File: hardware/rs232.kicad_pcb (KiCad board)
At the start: 2 copper layers, 45 x 35 mm, 33 parts, among them J1 DB9, P1 CON-SENSOR, P2 CONN_5, P3 CONN_5, U1 M24C64, U2 SC16IS740, U3 SP3232EBCN, U4 DRILL, U5 DRILL, U6 DRILL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

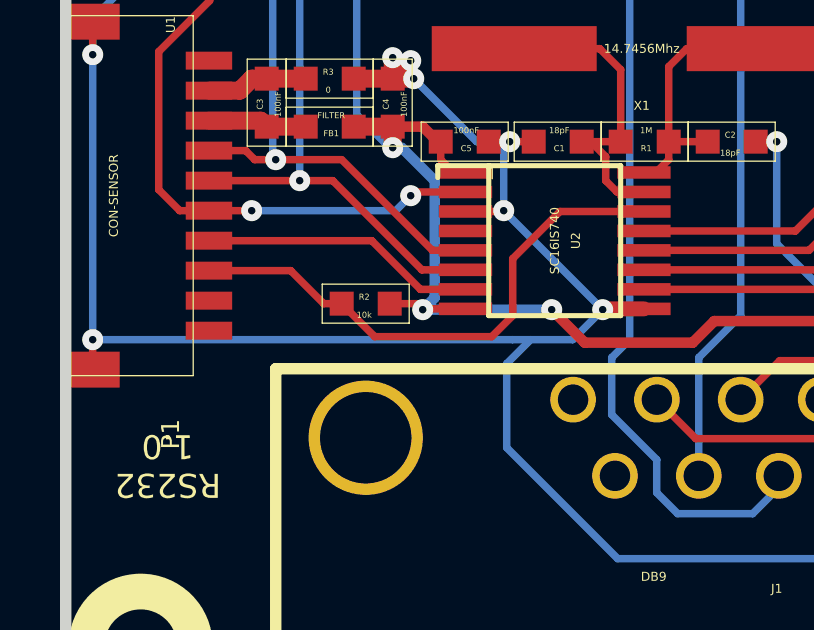
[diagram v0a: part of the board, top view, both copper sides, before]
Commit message: hardware adaption: fix reset to ground
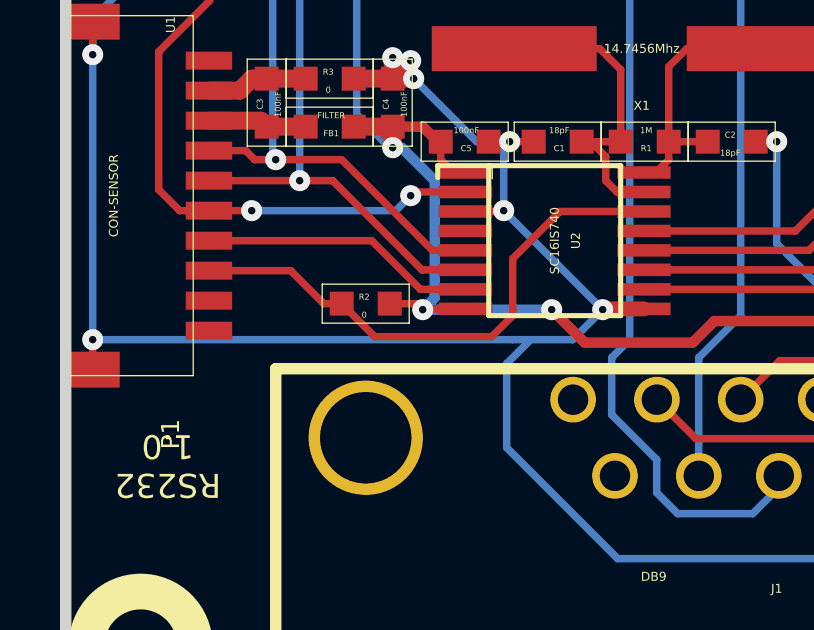
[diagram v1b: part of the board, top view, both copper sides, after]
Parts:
- R2: value 10k -> 0
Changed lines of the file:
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@@
-(kicad_pcb (version 4) (host pcbnew "(2015-03-18 BZR 5525)-product")
+(kicad_pcb (version 4) (host pcbnew 4.0.2+e4-6225~38~ubuntu15.10.1-stable)
   (general
     (links 68)
@@
       (effects (font (size 0.2 0.2) (thickness 0.05)))
     )
-    (fp_text value 10k (at 0.05 -0.375 180) (layer F.SilkS)
-      (effects (font (size 0.2 0.2) (thickness 0.05)))
-    )
+    (fp_text value 0 (at 0.05 -0.375 180) (layer F.SilkS)
+      (effects (font (size 0.2 0.2) (thickness 0.05)))
+    )
